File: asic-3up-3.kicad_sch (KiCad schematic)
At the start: 89 parts, among them J10 Conn_01x01, J11 Conn_01x01, J21 Conn_01x01, J22 Conn_01x01, U4 SN74AVC4T774, U5 25MHz, U66 MCP1824T-1202E/OT, U67 MCP1824T-1202E/OT, U68 MCP1824T-1202E/OT, U69 MCP1824T-0802E, U70 MCP1824T-0802E, U71 MCP1824T-0802E, U72 BM1362AC_MODE1, U73 BM1362AC_MODE0, U74 BM1362AC_MODE1

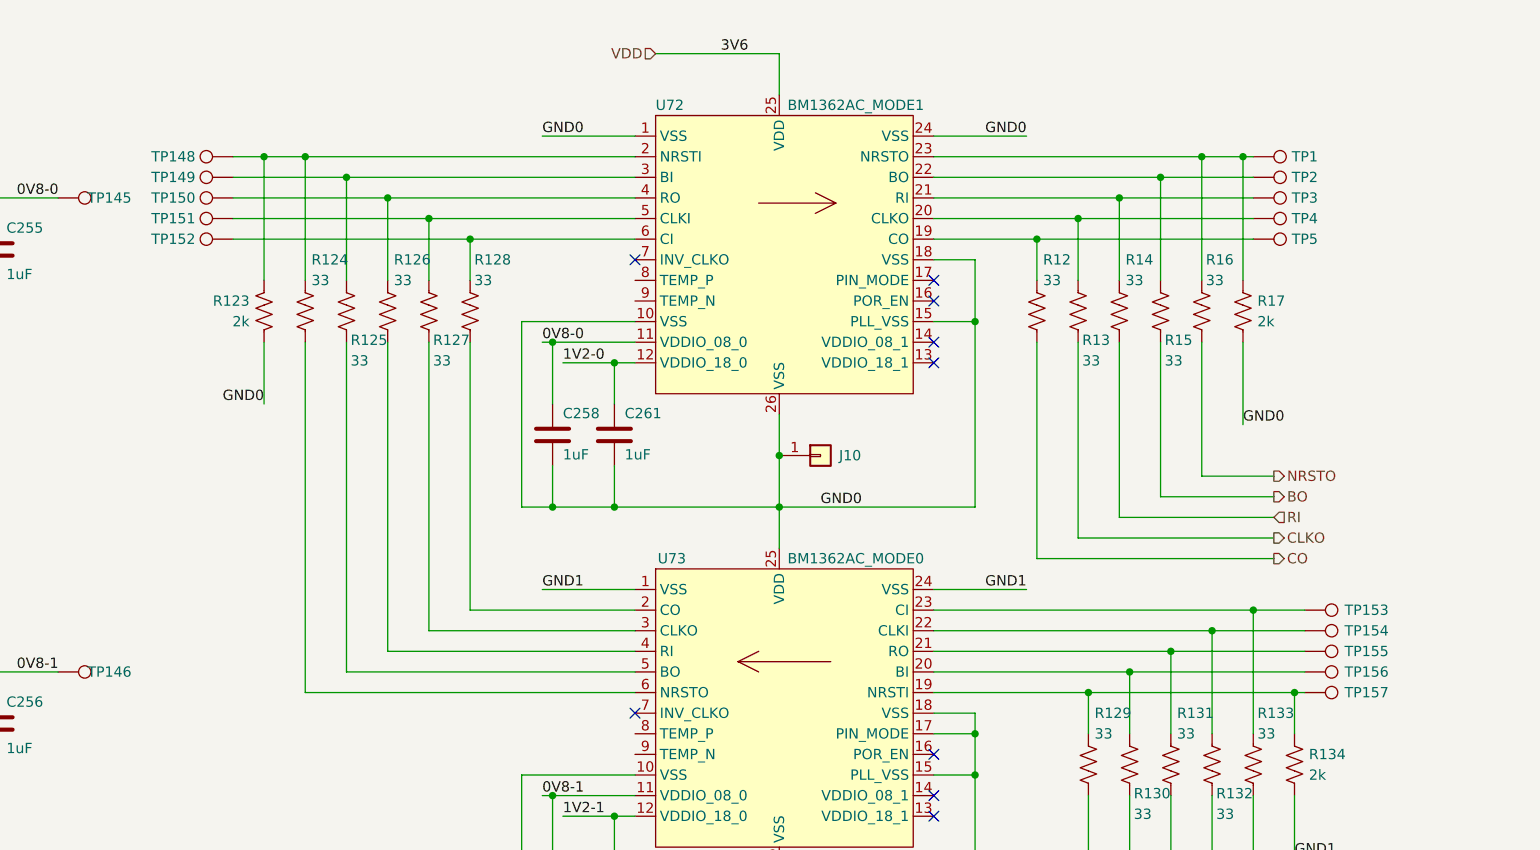
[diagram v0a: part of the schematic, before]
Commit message: all placed *almost* all routed
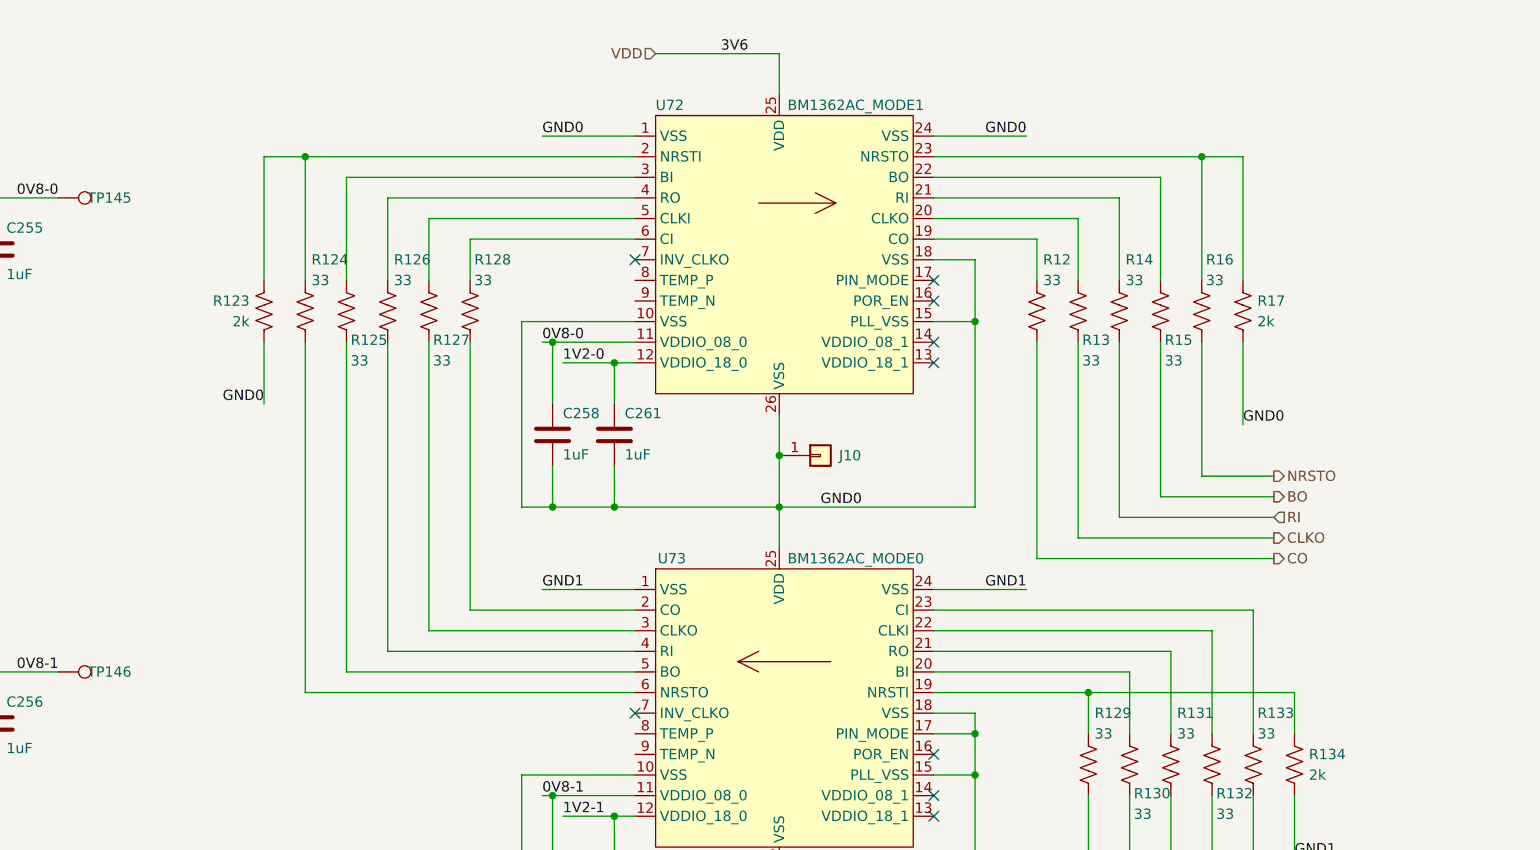
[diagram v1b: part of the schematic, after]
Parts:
- removed TP1, TP148, TP149, TP150, TP151, TP152, TP153, TP154, TP155, TP156, TP157, TP2, TP3, TP4, TP5: TestPoint, TestPoint:TestPoint_Pad_D1.0mm, symbol Connector:TestPoint

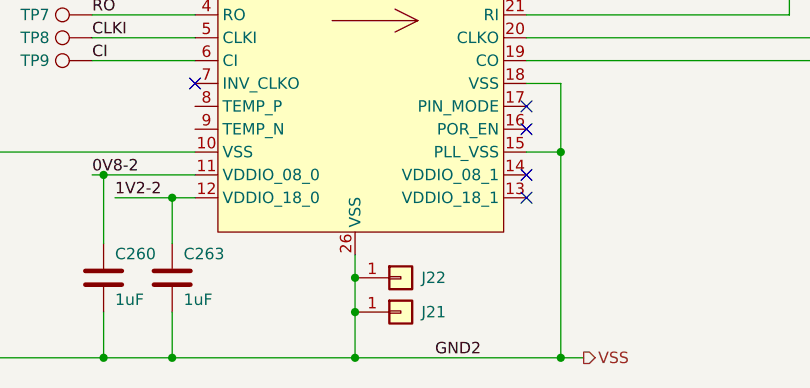
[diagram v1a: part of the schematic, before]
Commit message: cleaned up DRC
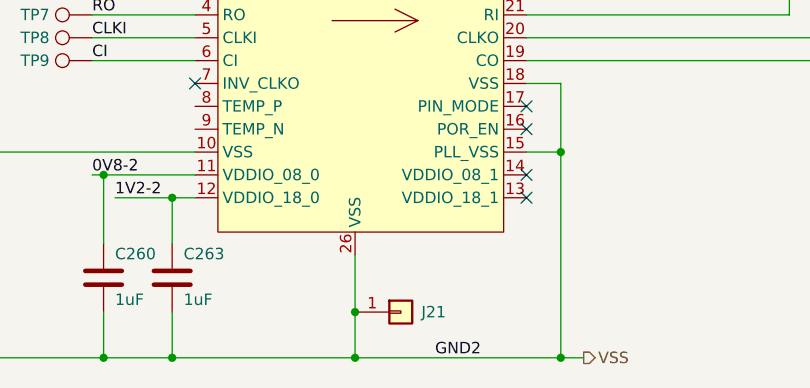
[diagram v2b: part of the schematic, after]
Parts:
- removed J22: Conn_01x01, emberone:14x9_powertab_L, symbol Connector_Generic:Conn_01x01
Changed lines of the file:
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@@
 	)
 	(junction
-		(at 248.92 246.38)
-		(diameter 0)
-		(color 0 0 0 0)
-	)
-	(junction
 		(at 220.98 255.27)
 		(diameter 0)
@@
 	(wire
 		(pts
-			(xy 248.92 246.38) (xy 248.92 250.19)
+			(xy 248.92 243.84) (xy 248.92 250.19)
 		)
 		(stroke
@@
 	(wire
 		(pts
-			(xy 248.92 243.84) (xy 248.92 246.38)
-		)
-		(stroke
-			(width 0)
-			(type default)
-		)
-	)
-	(wire
-		(pts
 			(xy 152.4 231.14) (xy 152.4 234.95)
 		)
@@
 					(unit 1)
 				)
-			)
-		)
-	)
-	(symbol
-		(lib_id "Connector_Generic:Conn_01x01")
-		(at 254 246.38 0)
-		(unit 1)
-		(exclude_from_sim no)
-		(in_bom yes)
-		(on_board yes)
-		(dnp no)
-		(property "Reference" "J22"
-			(at 256.286 246.38 0)
-			(effects
-				(font
-					(size 1.27 1.27)
-				)
-				(justify left)
-			)
-		)
-		(property "Value" "Conn_01x01"
-			(at 256.54 247.6499 0)
-			(effects
-				(font
-					(size 1.27 1.27)
-				)
-				(justify left)
-				(hide yes)
-			)
-		)
-		(property "Footprint" "emberone:14x9_powertab_L"
-			(at 254 246.38 0)
-			(effects
-				(font
-					(size 1.27 1.27)
-				)
-				(hide yes)
-			)
-		)
-		(property "Datasheet" "~"
-			(at 254 246.38 0)
-			(effects
-				(font
-					(size 1.27 1.27)
-				)
-				(hide yes)
-			)
-		)
-		(property "Description" "powertab"
-			(at 254 246.38 0)
-			(effects
-				(font
-					(size 1.27 1.27)
-				)
-				(hide yes)
-			)
-		)
-		(pin "1"
-		)
-		(instances
-			(project "emberone"
-				(path "/b036224c-4cdf-48cc-81df-19bc5283ebd2/75fd7cab-4b1e-4fa4-8631-02e52962bbf8"
-					(reference "J22")
-					(unit 1)
-				)

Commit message: changed the RP2040 Flash to a QSPI version. Added DK RP2040 crystal. Added LED. Added some 3D models. Generated BOM. Generated Gerbers
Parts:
- R12, R124, R125, R126, R127, R128, R129, R13, R130, R131, R132, R133, R14, R15, R16: DK (none) -> 311-33.0LRCT-ND; PARTNO (none) -> RC0402FR-0733RL
- R123, R134, R17: DK (none) -> 311-2KLRCT-ND; PARTNO (none) -> RC0402FR-072KL
- R18: DK (none) -> 311-10.0KLRCT-ND; PARTNO (none) -> RC0402FR-0710KL

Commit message: generated updated gerbers
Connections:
- no-connect marks 21 -> 27
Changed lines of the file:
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@@
 	)
 	(no_connect
+		(at 231.14 173.99)
+	)
+	(no_connect
 		(at 267.97 229.87)
 	)
@@
 	)
 	(no_connect
+		(at 231.14 227.33)
+	)
+	(no_connect
 		(at 66.04 168.91)
 	)
@@
 	)
 	(no_connect
+		(at 231.14 171.45)
+	)
+	(no_connect
+		(at 231.14 229.87)
+	)
+	(no_connect
 		(at 267.97 173.99)
 	)
@@
 	)
 	(no_connect
+		(at 231.14 118.11)
+	)
+	(no_connect
+		(at 231.14 115.57)
+	)
+	(no_connect
 		(at 267.97 179.07)
 	)
@@
 		)
 	)
-	(label "3V6"
+	(label "VDD"
 		(at 354.33 106.68 180)
 		(fields_autoplaced yes)
@@
 		)
 	)
-	(label "3V6"
+	(label "VDD"
 		(at 245.11 87.63 180)
 		(fields_autoplaced yes)
